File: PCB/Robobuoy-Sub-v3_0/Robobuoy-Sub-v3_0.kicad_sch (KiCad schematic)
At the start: 0 parts

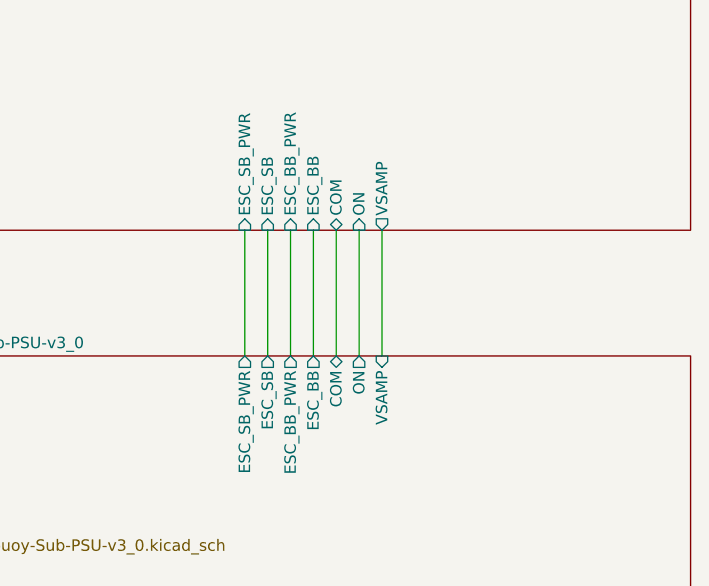
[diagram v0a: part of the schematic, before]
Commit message: PCB 3.0 almoste finished Imon calculation added
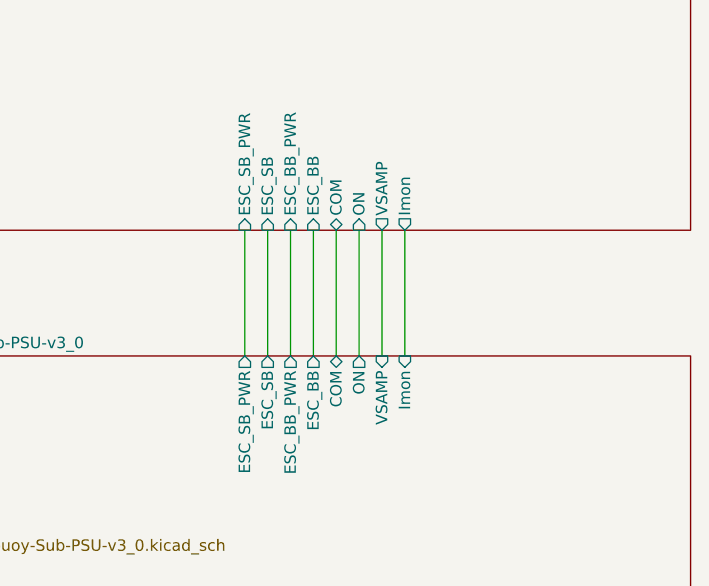
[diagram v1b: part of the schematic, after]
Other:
- sheet CPU ports: added Imon; removed none
- sheet Robobuoy-Sub-PSU-v3_0 ports: added Imon; removed none
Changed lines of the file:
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@@
+	(wire
+		(pts
+			(xy 158.75 101.6) (xy 158.75 115.57)
+		)
+		(stroke
+			(width 0)
+			(type default)
+		)
+	)
 	(wire
 		(pts
@@
 			)
 		)
+		(pin "Imon" output
+			(at 158.75 101.6 270)
+			(effects
+				(font
+					(size 1.27 1.27)
+				)
+				(justify left)
+			)
+		)
 		(instances
 			(project "Robobuoy-Sub-v3_0"
@@
 			(effects
 				(font
+					(size 1.27 1.27)
+				)
+				(justify right)
+			)
+		)
+		(pin "Imon" input
+			(at 158.75 115.57 90)
+			(effects
+				(font

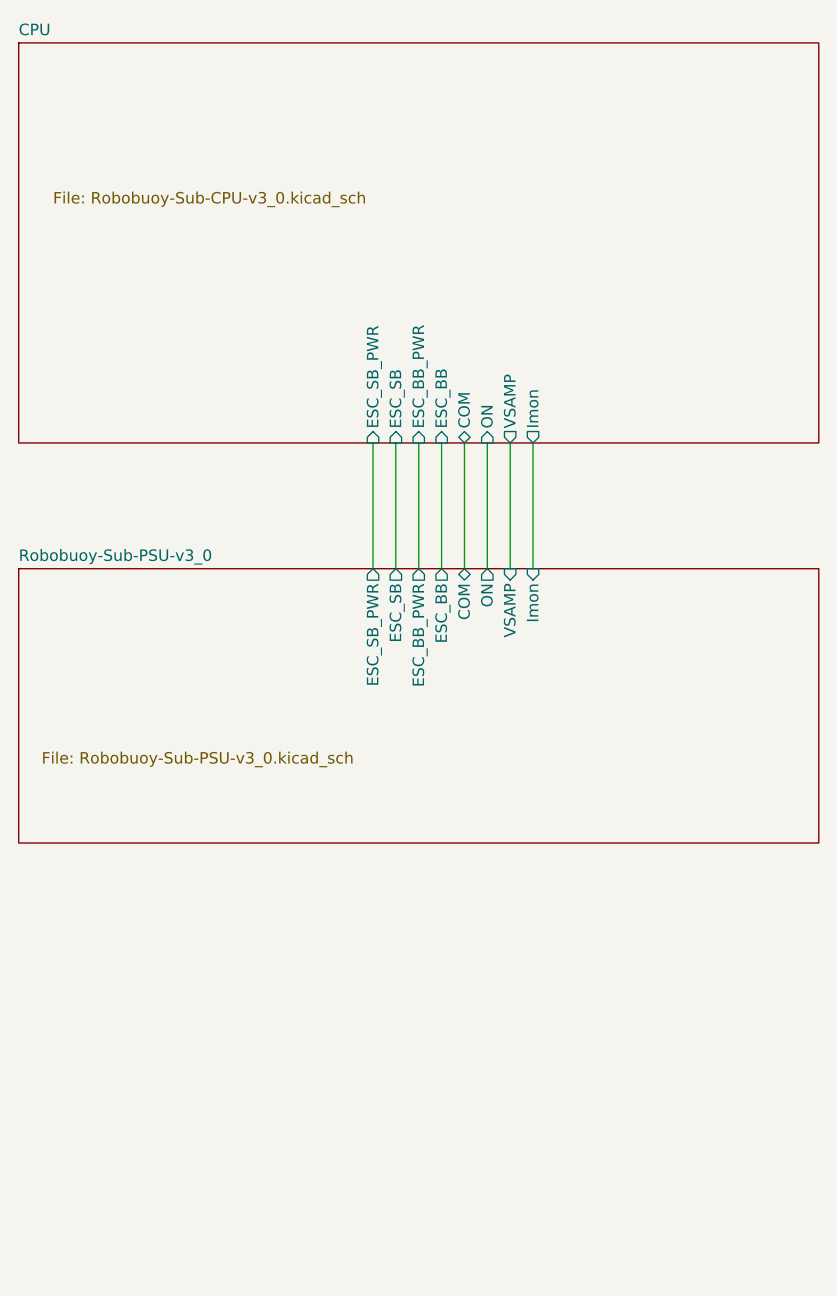
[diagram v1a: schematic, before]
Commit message: Simulation added bms Little improvements BMS Resistor divider added on the gate of the mosfet (Limmeded to +/-20V could be 30V during charging)
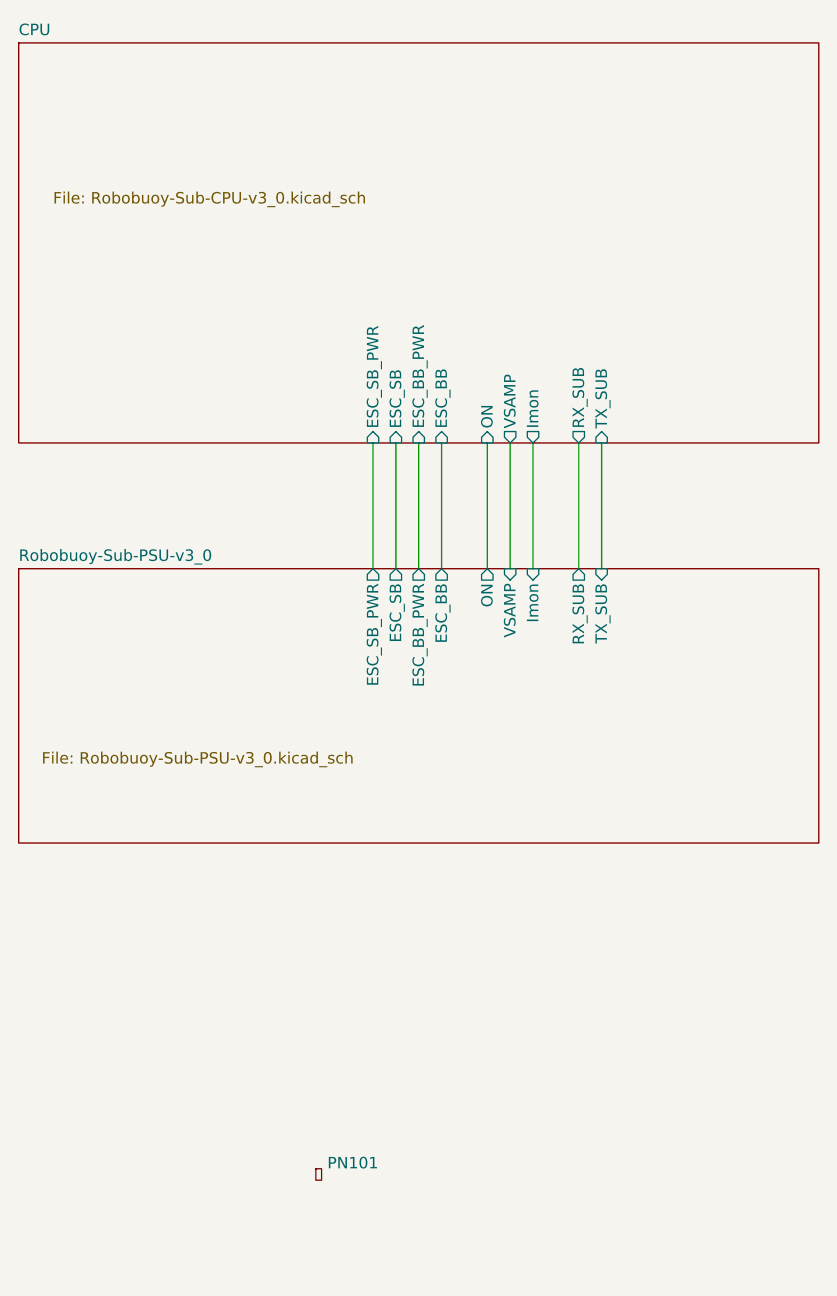
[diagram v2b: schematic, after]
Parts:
- added PN101: ~, PCM_JLCPCB:Part_Num_JLCPCB, symbol PCM_JLCPCB-Manufacturing:Part Number, PCM_JLCPCB, 0.8x0.15mm
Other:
- sheet CPU ports: added RX_SUB, TX_SUB; removed COM
- sheet Robobuoy-Sub-PSU-v3_0 ports: added RX_SUB, TX_SUB; removed COM
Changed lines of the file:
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@@
+	(wire
+		(pts
+			(xy 166.37 101.6) (xy 166.37 115.57)
+		)
+		(stroke
+			(width 0)
+			(type default)
+		)
+	)
 	(wire
 		(pts
@@
 	(wire
 		(pts
-			(xy 151.13 101.6) (xy 151.13 115.57)
+			(xy 163.83 101.6) (xy 163.83 115.57)
 		)
 		(stroke
@@
 			(width 0)
 			(type default)
+		)
+	)
+	(symbol
+		(lib_id "PCM_JLCPCB-Manufacturing:Part Number, PCM_JLCPCB, 0.8x0.15mm")
+		(at 134.62 182.88 0)
+		(unit 1)
+		(exclude_from_sim no)
+		(in_bom yes)
+		(on_board yes)
+		(dnp no)
+		(fields_autoplaced yes)
+		(property "Reference" "PN101"
+			(at 135.89 181.6099 0)
+			(effects
+				(font
+					(size 1.27 1.27)
+				)
+				(justify left)
+			)
+		)
+		(property "Value" "~"
+			(at 135.89 184.1499 0)
+			(effects
+				(font
+					(size 1.27 1.27)
+				)
+				(justify left)
+			)
+		)
+		(property "Footprint" "PCM_JLCPCB:Part_Num_JLCPCB"
+			(at 134.62 182.88 0)
+			(effects
+				(font
+					(size 1.27 1.27)
+				)
+				(hide yes)
+			)
+		)
+		(property "Datasheet" "https://jlcpcb.com/help/article/How-to-remove-order-number-from-your-PCB"
+			(at 134.62 182.88 0)
+			(effects
+				(font
+					(size 1.27 1.27)
+				)
+				(hide yes)
+			)
+		)
+		(property "Description" "To indicate the location, simply add the text \"JLCJLCJLCJLC\" to the silk layer and select the \"Specify a location\" option when placing your order. Please note that if this option is not chosen, we may not notice that you have added the text.   Note: Use only \"JLCJLCJLCJLC\" without any additional characters. The font size should be larger than 0.8mm in height and 0.15mm in width."
+			(at 134.62 182.88 0)
+			(effects
+				(font
+					(size 1.27 1.27)
+				)
+				(hide yes)
+			)
+		)
+		(instances
+			(project ""
+				(path "/b4d50f7c-16b2-4c5a-bb6a-7ca43079286e"
+					(reference "PN101")
+					(unit 1)
+				)
+			)
 		)
 	)
@@
 			)
 		)
-		(pin "COM" bidirectional
-			(at 151.13 101.6 270)
-			(effects
-				(font
-					(size 1.27 1.27)
-				)
-				(justify left)
-			)
-		)
 		(pin "ESC_BB" input
 			(at 148.59 101.6 270)
@@
 		(pin "Imon" output
 			(at 158.75 101.6 270)
+			(effects
+				(font
+					(size 1.27 1.27)
+				)
+				(justify left)
+			)
+		)
+		(pin "RX_SUB" output
+			(at 163.83 101.6 270)
+			(effects
+				(font
+					(size 1.27 1.27)
+				)
+				(justify left)
+			)
+		)
+		(pin "TX_SUB" input
+			(at 166.37 101.6 270)
 			(effects
 				(font
@@
 			)
 		)
-		(pin "COM" bidirectional
-			(at 151.13 115.57 90)
-			(effects
-				(font
-					(size 1.27 1.27)
-				)
-				(justify right)
-			)
-		)
 		(pin "ESC_BB" output
 			(at 148.59 115.57 90)
@@
 			(effects
 				(font
+					(size 1.27 1.27)
+				)
+				(justify right)
+			)
+		)
+		(pin "RX_SUB" output
+			(at 163.83 115.57 90)
+			(effects
+				(font
+					(size 1.27 1.27)
+				)
+				(justify right)
+			)
+		)
+		(pin "TX_SUB" input
+			(at 166.37 115.57 90)
+			(effects
+				(font

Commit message: Heel veel AI veranderingen.
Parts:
- PN101: value ~ -> Partnumber JLCPCB
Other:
- moved on the sheet: PN101
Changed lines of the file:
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@@
 	(symbol
 		(lib_id "PCM_JLCPCB-Manufacturing:Part Number, PCM_JLCPCB, 0.8x0.15mm")
-		(at 134.62 182.88 0)
+		(at 153.67 191.77 0)
 		(unit 1)
 		(exclude_from_sim no)
@@
 		(fields_autoplaced yes)
 		(property "Reference" "PN101"
-			(at 135.89 181.6099 0)
+			(at 154.94 190.4999 0)
 			(effects
 				(font
@@
 			)
 		)
-		(property "Value" "~"
-			(at 135.89 184.1499 0)
+		(property "Value" "Partnumber JLCPCB"
+			(at 154.94 193.0399 0)
 			(effects
 				(font
@@
 		)
 		(property "Footprint" "PCM_JLCPCB:Part_Num_JLCPCB"
-			(at 134.62 182.88 0)
+			(at 153.67 191.77 0)
 			(effects
 				(font
@@
 		)
 		(property "Datasheet" "https://jlcpcb.com/help/article/How-to-remove-order-number-from-your-PCB"
-			(at 134.62 182.88 0)
+			(at 153.67 191.77 0)
 			(effects
 				(font
@@
 		)
 		(property "Description" "To indicate the location, simply add the text \"JLCJLCJLCJLC\" to the silk layer and select the \"Specify a location\" option when placing your order. Please note that if this option is not chosen, we may not notice that you have added the text.   Note: Use only \"JLCJLCJLCJLC\" without any additional characters. The font size should be larger than 0.8mm in height and 0.15mm in width."
-			(at 134.62 182.88 0)
+			(at 153.67 191.77 0)
 			(effects
 				(font
